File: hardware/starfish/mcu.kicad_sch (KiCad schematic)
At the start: 38 parts, among them SW1 BOOTSEL, U3 RP2040, U4 W25Q128JVS, Y1 12MHz

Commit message: First pass at schematic for starfish
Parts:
- added R?: 1k, Resistor_SMD:R_0402_1005Metric_Pad0.72x0.64mm_HandSolder, symbol Device:R_US
- added SW?: RESET, winterbloom:Tactile_Switch_4.2mm, symbol winterbloom:Tactile_Switch
- R?: renamed from R28; footprint Resistor_SMD:R_0603_1608Metric_Pad0.98x0.95mm_HandSolder -> (none); Rating 200mW -> 63mW
- R?: renamed from R10; Rating 200mW -> 63mW
- renumbered C12 to C?, C17 to C?, C20 to C?, C24 to C?, C19 to C?, C10 to C?, C15 to C?, C11 to C?, C21 to C?, C18 to C?, C25 to C?, C23 to C?, C13 to C?, C16 to C?, C14 to C?, C26 to C?, D4 to D?, D1 to D?, R11 to R?, R4 to R?, R12 to R?, R5 to R?, R6 to R?, R8 to R?, R9 to R?, R7 to R?, SW1 to SW?, TP9 to TP?, TP8 to TP?, TP5 to TP?, TP17 to TP?, TP6 to TP?, TP7 to TP?, U3 to U?, U4 to U?, Y1 to Y?
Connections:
- net GND: now also SW?.2
- net RUN: now also R?.2
- net BLTOUCH_CONTROL: no longer names the net of U?.6 (GPIO4)
- net BLTOUCH_STATUS: no longer names the net of U?.7 (GPIO5)
- net QWIIC_SCL renamed I2C_SCL
- net QWIIC_SDA renamed I2C_SDA
- new net: R?.1, SW?.1
- no-connect marks 6 -> 8
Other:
- note added: "* Make sure 1u caps are close to pin 44 (VREG_IN) & 45 (VREG_OUT)"
- note added: "* Make sure R6 & R7 are close to pins 46 & 47 (USB D- & D+) * 1kΩ resistor on TMC UART TX per TMC2209 datasheet Figure 4.1 * ACT_LED can be re-assigned to any free pin * Check RP2040 pin mux before re-assigning UART & I2C pins * Crystal requires extra start up time"
- note added: "* Verify passives with actual crystal"
- note added: "LEDs, boot, and reset buttons"
- note added: "Test points"
- note removed: "* Make sure C18 is close to pin 44 (VREG_IN) * Make sure C19 is close to pin 45 (VREG_OUT)"
- note removed: "* Verify R1, C23, and C24 values with actual crystal"
- note removed: "Debug, boot select, and LED"
- note removed: "Schematic notes: * Make sure R6 & R7 are close to pins 46 & 47 (USB D- & D+) * 1kΩ resistor on TMC UART TX per TMC2209 datasheet Figure 4.1 * ACT_LED can be re-assigned to any free pin * Check RP2040 pin mux before re-assigning UART & I2C pins * Crystal requires extra start up time"
- title: Jellyfish -> Starfish
- moved on the sheet: C?, D?, R?, SW?, TP?, U?, Y?

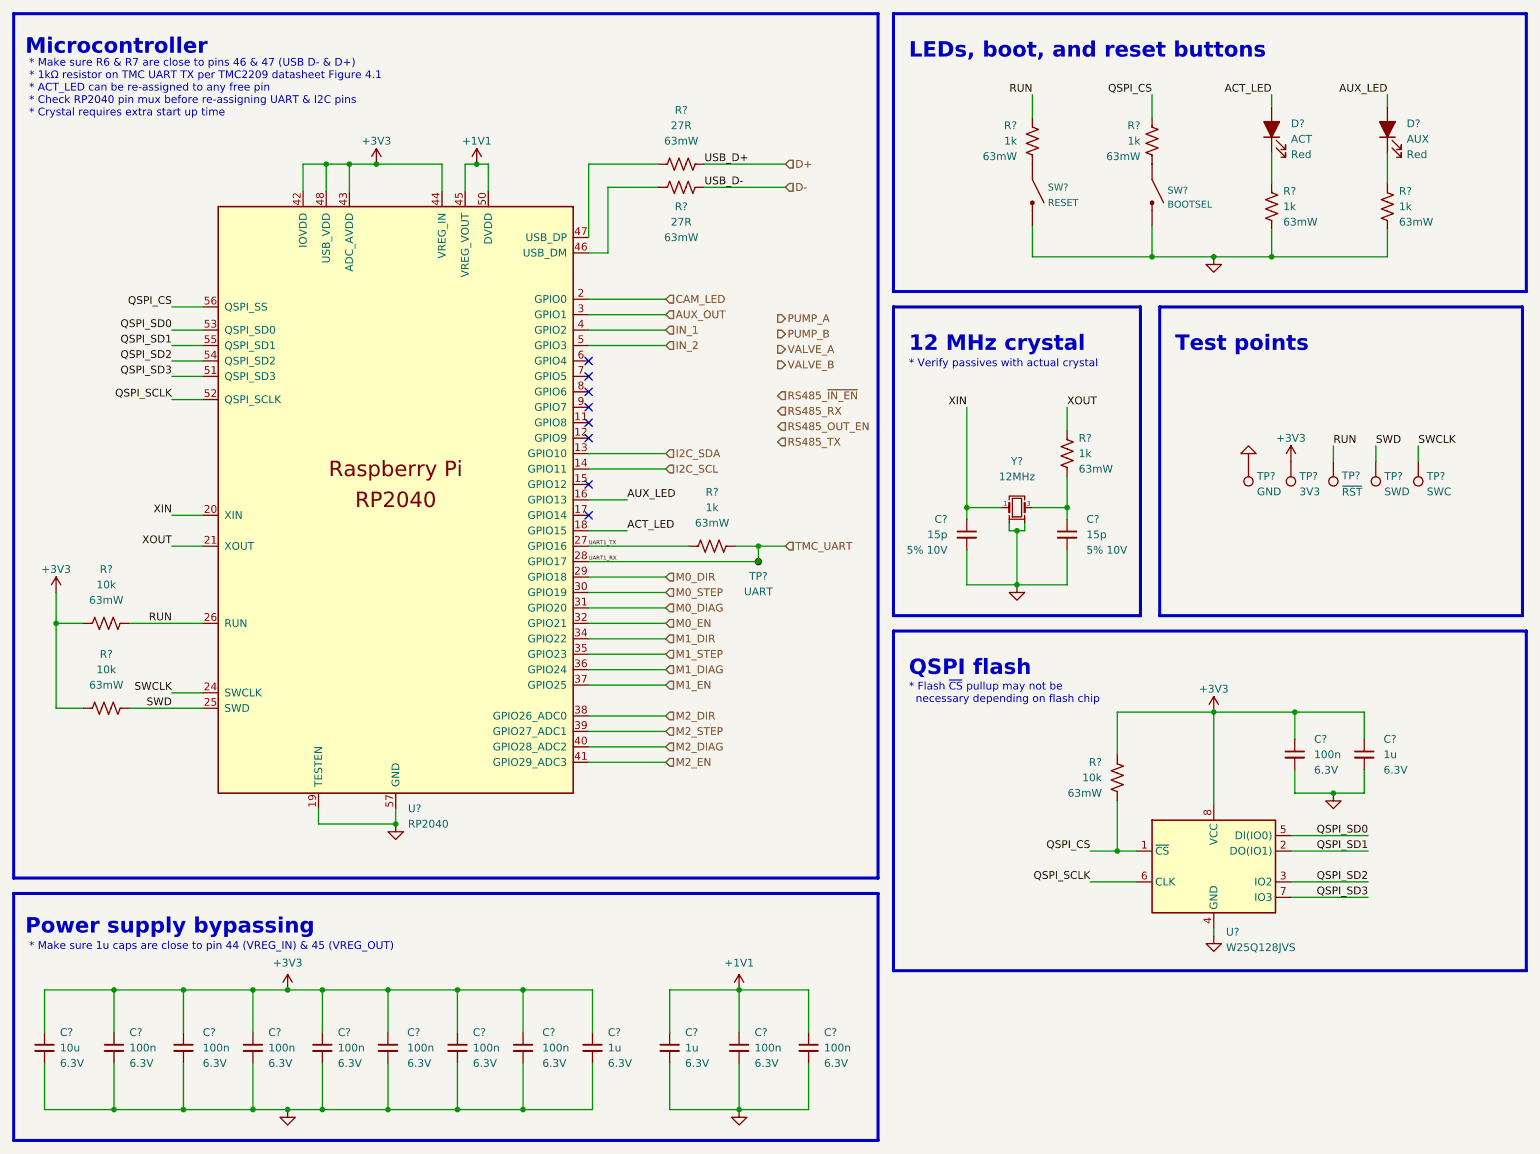
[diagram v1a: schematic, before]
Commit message: Mostly finished starfish schematic, ready for layout!
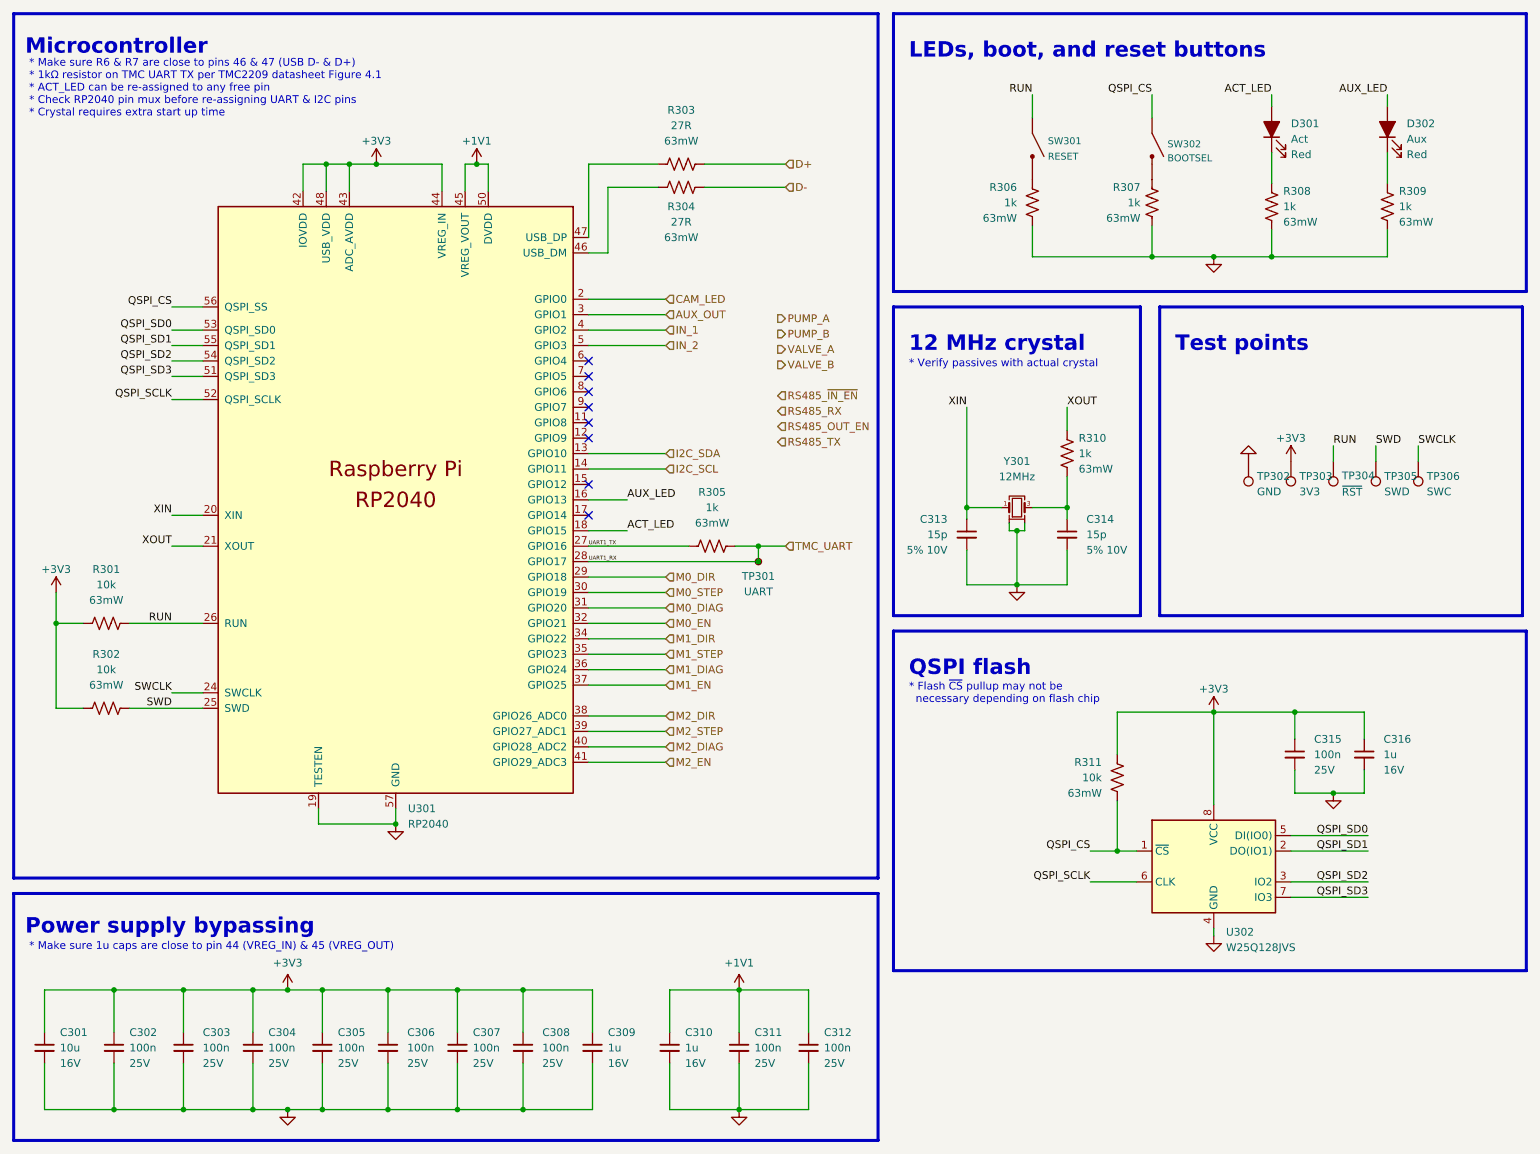
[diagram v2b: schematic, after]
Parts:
- C301: renamed from C?; footprint Capacitor_SMD:C_0805_2012Metric_Pad1.18x1.45mm_HandSolder -> winterbloom:C_0805_HandSolder; Rating 6.3V -> 16V
- C302, C303, C304, C305, C306, C307, C308, C311, C312, C315: renamed from C?; footprint Capacitor_SMD:C_0402_1005Metric_Pad0.74x0.62mm_HandSolder -> winterbloom:C_0402_HandSolder; Rating 6.3V -> 25V
- C309, C310, C316: renamed from C?; footprint Capacitor_SMD:C_0402_1005Metric_Pad0.74x0.62mm_HandSolder -> winterbloom:C_0402_HandSolder; Rating 6.3V -> 16V
- C313, C314: renamed from C?; footprint Capacitor_SMD:C_0402_1005Metric_Pad0.74x0.62mm_HandSolder -> winterbloom:C_0402_HandSolder
- D301: renamed from D?; value ACT -> Act
- D302: renamed from D?; value AUX -> Aux
- R301, R302, R303, R304, R305, R306, R307, R310, R311: renamed from R?; footprint Resistor_SMD:R_0402_1005Metric_Pad0.72x0.64mm_HandSolder -> winterbloom:R_0402_HandSolder
- R308: renamed from R?; footprint Resistor_SMD:R_0603_1608Metric_Pad0.98x0.95mm_HandSolder -> winterbloom:R_0402_HandSolder; mpn (none) -> RC0402JR-071KL
- R309: renamed from R?; footprint (none) -> winterbloom:R_0402_HandSolder; mpn (none) -> RC0402JR-071KL
- SW301, SW302: renamed from SW?; MPN (none) -> MF-SW-TACT-4.2MM, MF-SW-TACT-6MM; mpn MF-SW-TACT-4.2MM, MF-SW-TACT-6MM -> (none)
- TP301, TP302, TP303, TP304, TP305, TP306: renamed from TP?; mpn n/a -> (none)
- U301: renamed from U?; symbol MCU_RaspberryPi_RP2040:RP2040 -> winterbloom:RP2040
- gave numbers to parts that had none: 2
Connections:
- net GND: now also R306.1, R307.1; no longer SW301.2, SW302.2
- net QSPI_CS: now also SW302.1; no longer R307.2
- net RUN: now also SW301.1; no longer R306.2
- new net: R306.2, SW301.2
- new net: R307.2, SW302.2
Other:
- moved on the sheet: R306, R307, SW301, SW302

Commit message: First pass at layout and routing
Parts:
- removed TP302: GND, TestPoint:TestPoint_Pad_D1.0mm, symbol Connector:TestPoint
- removed TP303: 3V3, TestPoint:TestPoint_Pad_D1.0mm, symbol Connector:TestPoint
- removed TP304: ~{RST}, TestPoint:TestPoint_Pad_D1.0mm, symbol Connector:TestPoint
- removed TP305: SWD, TestPoint:TestPoint_Pad_D1.0mm, symbol Connector:TestPoint
- removed TP306: SWC, TestPoint:TestPoint_Pad_D1.0mm, symbol Connector:TestPoint
- added J1: SWD, winterbloom:Connector_Cortex_Debug_IDC_2x05_P1.27mm_Vertical_Shrouded_SMD, symbol winterbloom:Conn_SWD
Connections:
- net +3V3: now also J1.1 (VCC)
- net ACT_LED: now also U301.7 (GPIO5); no longer U301.18 (GPIO15)
- net AUX_LED: now also U301.6 (GPIO4); no longer U301.16 (GPIO13)
- net AUX_OUT: now also U301.17 (GPIO14); no longer U301.3 (GPIO1)
- net CAM_LED: now also U301.18 (GPIO15); no longer U301.2 (GPIO0)
- net GND: now also J1.3 (GND), J1.5 (GND), J1.9 (GNDDetect)
- net I2C_SCL: now also U301.9 (GPIO7); no longer U301.14 (GPIO11)
- net I2C_SDA: now also U301.8 (GPIO6); no longer U301.13 (GPIO10)
- net IN_1: now also U301.15 (GPIO12); no longer U301.4 (GPIO2)
- net IN_2: now also U301.16 (GPIO13); no longer U301.5 (GPIO3)
- net M0_DIAG: now also U301.40 (GPIO28_ADC2); no longer U301.31 (GPIO20)
- net M0_DIR: now also U301.38 (GPIO26_ADC0); no longer U301.29 (GPIO18)
- net M0_EN: now also U301.41 (GPIO29_ADC3); no longer U301.32 (GPIO21)
- net M0_STEP: now also U301.39 (GPIO27_ADC1); no longer U301.30 (GPIO19)
- net M2_DIAG: now also U301.31 (GPIO20); no longer U301.40 (GPIO28_ADC2)
- net M2_DIR: now also U301.29 (GPIO18); no longer U301.38 (GPIO26_ADC0)
- net M2_EN: now also U301.32 (GPIO21); no longer U301.41 (GPIO29_ADC3)
- net M2_STEP: now also U301.30 (GPIO19); no longer U301.39 (GPIO27_ADC1)
- net PUMP_A: now also U301.2 (GPIO0)
- net PUMP_B: now also U301.3 (GPIO1)
- net RS485_OUT_EN: now also U301.14 (GPIO11)
- net RS485_RX: now also U301.12 (GPIO9)
- net RS485_TX: now also U301.11 (GPIO8)
- net RS485_~{IN_EN}: now also U301.13 (GPIO10)
- net RUN: now also J1.10 (~{RESET})
- net SWCLK: now also J1.4 (SWCLK)
- net SWD: now also J1.2 (SWDIO)
- net TMC_UART: now also R305.1; no longer R305.2
- net VALVE_A: now also U301.4 (GPIO2)
- net VALVE_B: now also U301.5 (GPIO3)
- net UART1_TX renamed UART0_TX
- net UART0_TX: now also R305.2; no longer R305.1
- no-connect marks 8 -> 1
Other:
- note added: "SWD"
- note removed: "Test points"
- moved on the sheet: C313, C314, R301, R302, R303, R304, R305, R310, TP301, U301, Y301

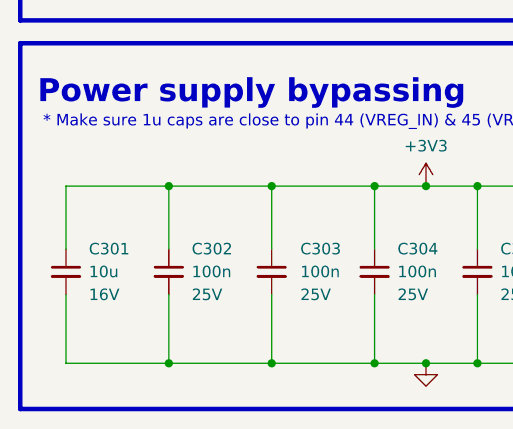
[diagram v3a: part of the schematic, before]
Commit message: Run through purchasing, update some cap sizes
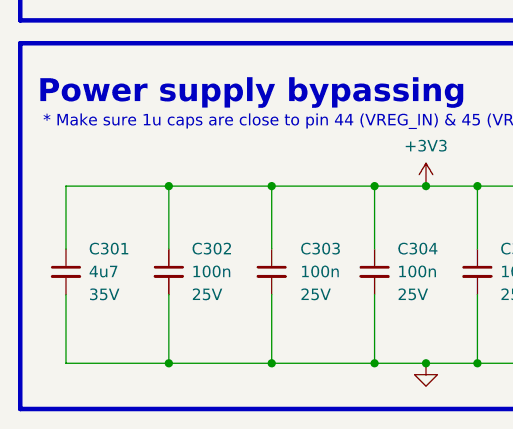
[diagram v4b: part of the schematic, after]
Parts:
- C301: value 10u -> 4u7; Rating 16V -> 35V; mpn CL32B106KBJNNNE -> CL21A475KLCLQNC
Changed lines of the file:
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@@
       (effects (font (size 1.27 1.27)) (justify left))
     )
-    (property "Value" "10u" (id 1) (at 22.86 185.4262 0)
+    (property "Value" "4u7" (id 1) (at 22.86 185.4262 0)
       (effects (font (size 1.27 1.27)) (justify left))
     )
@@
       (effects (font (size 1.27 1.27)) hide)
     )
-    (property "mpn" "CL32B106KBJNNNE" (id 4) (at 20.32 185.42 0)
+    (property "mpn" "CL21A475KLCLQNC" (id 4) (at 20.32 185.42 0)
       (effects (font (size 1.27 1.27)) hide)
     )
-    (property "Rating" "16V" (id 5) (at 22.86 187.9662 0)
+    (property "Rating" "35V" (id 5) (at 22.86 187.9662 0)
       (effects (font (size 1.27 1.27)) (justify left))
     )
